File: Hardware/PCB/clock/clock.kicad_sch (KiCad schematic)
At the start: 51 parts, among them J1 Synth_power_2x5, J2 AudioJack2, J3 AudioJack2, J4 AudioJack2, J5 AudioJack2, J6 AudioJack2, J7 AudioJack2, Q1 2N3904, SW1 RotaryEncoder, SW2 SW_Push, U1 40106

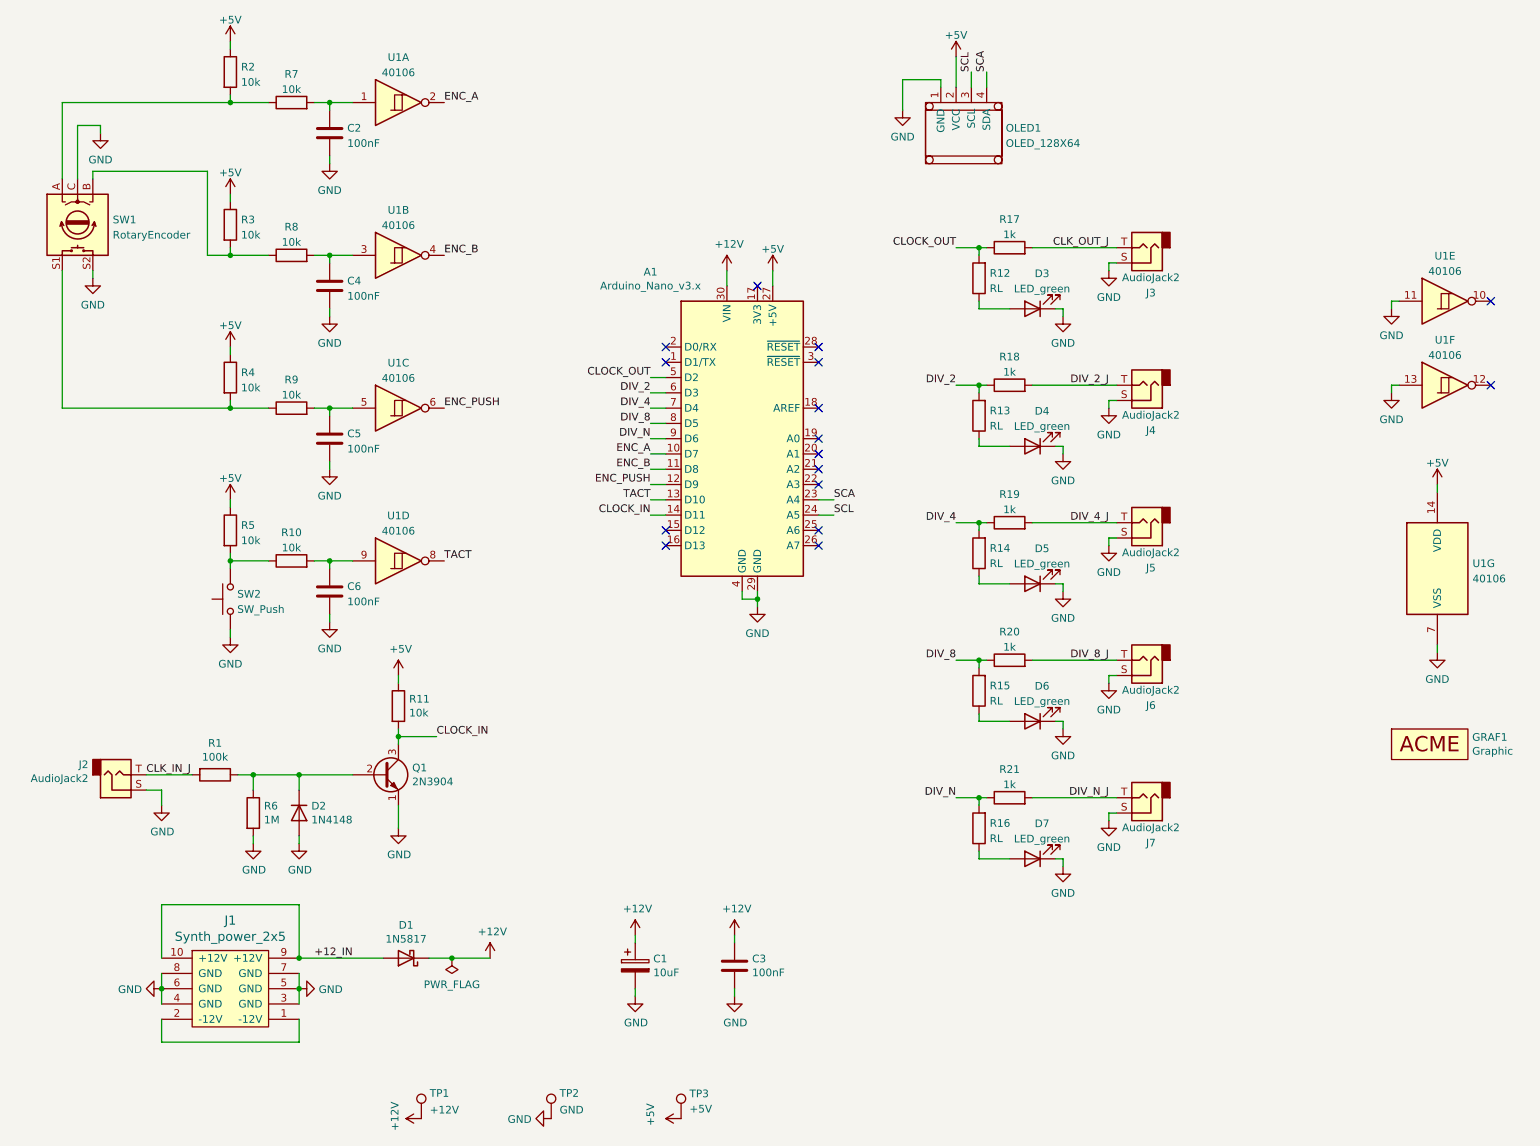
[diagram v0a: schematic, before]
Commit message: Invert clock in; fill in README; software improvements; rm notes
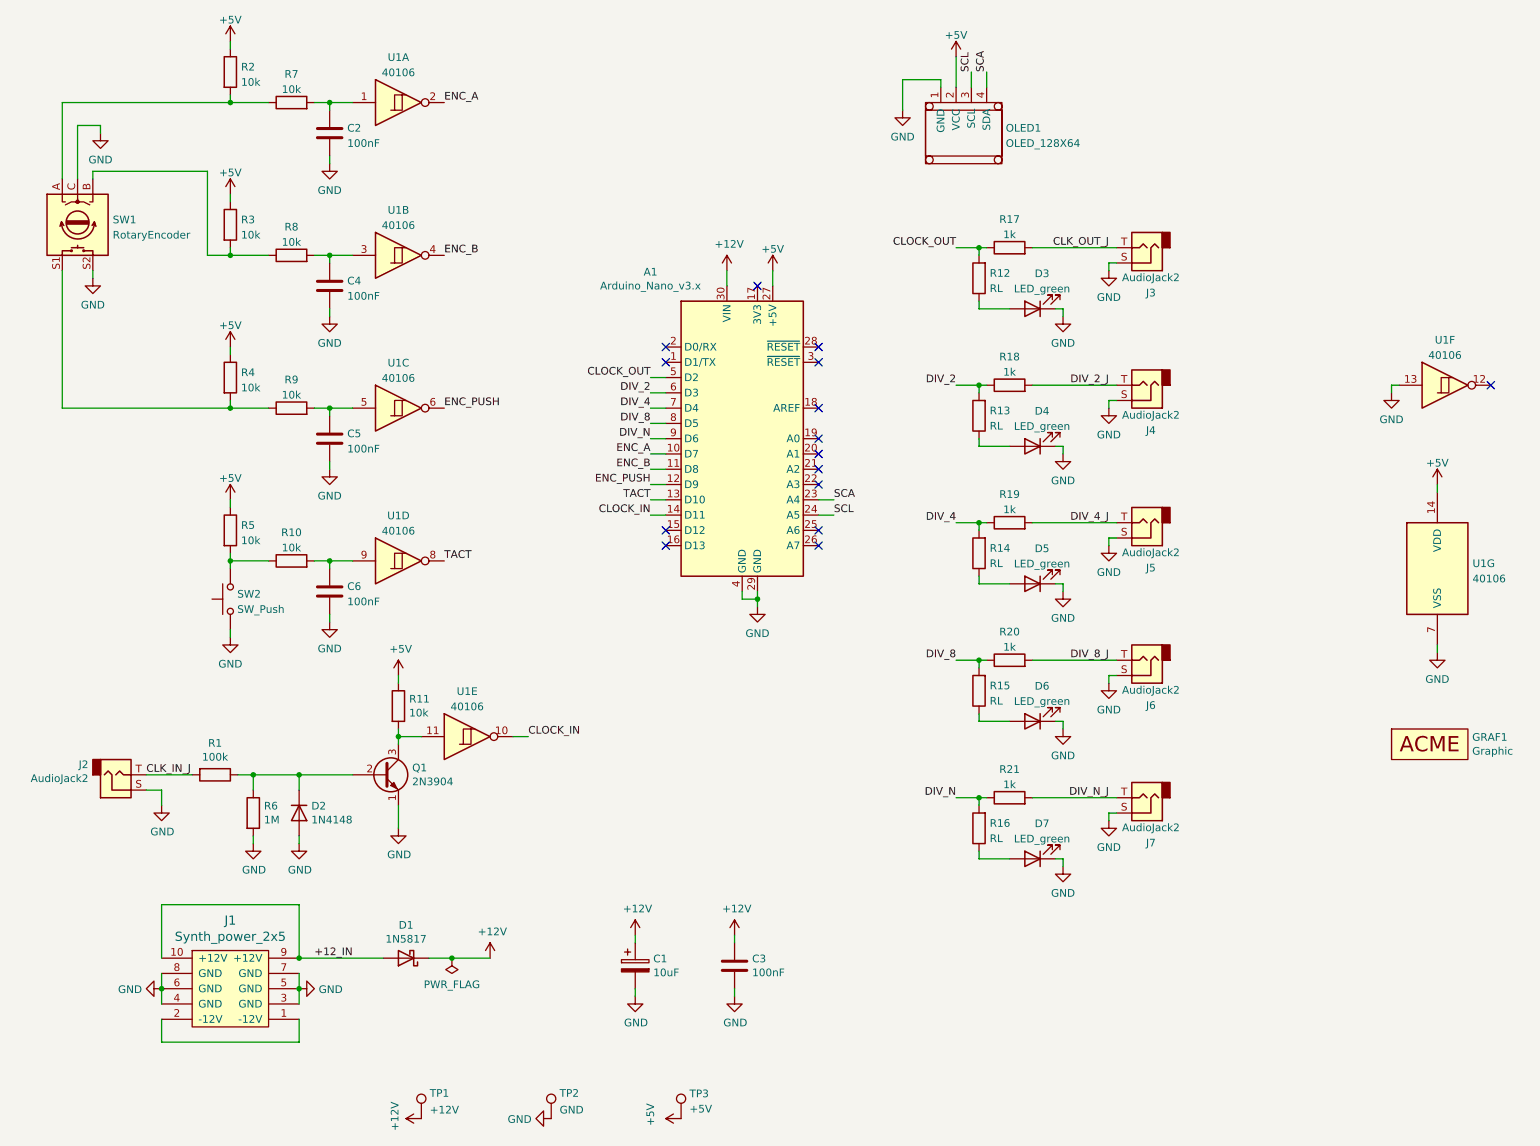
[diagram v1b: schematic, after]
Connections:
- net CLOCK_IN: now also U1.10; no longer Q1.3 (C), R11.2
- net GND: no longer U1.11
- new net: Q1.3 (C), R11.2, U1.11
- no-connect marks 16 -> 15
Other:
- moved on the sheet: U1E
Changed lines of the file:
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@@
   (no_connect (at 123.19 101.6))
   (no_connect (at 260.35 77.47))
-  (no_connect (at 260.35 63.5))
   (no_connect (at 138.43 60.96))
   (wire (pts (xy 22.86 58.42) (xy 22.86 81.28))
@@
     (stroke (width 0) (type default) (color 0 0 0 0))
   )
-  (wire (pts (xy 245.11 63.5) (xy 243.84 63.5))
-    (stroke (width 0) (type default) (color 0 0 0 0))
-  )
   (wire (pts (xy 171.45 123.19) (xy 175.26 123.19))
     (stroke (width 0) (type default) (color 0 0 0 0))
@@
     (stroke (width 0) (type default) (color 0 0 0 0))
   )
+  (wire (pts (xy 100.33 135.89) (xy 97.79 135.89))
+    (stroke (width 0) (type default) (color 0 0 0 0))
+  )
   (wire (pts (xy 50.8 118.11) (xy 50.8 119.38))
     (stroke (width 0) (type default) (color 0 0 0 0))
@@
     (stroke (width 0) (type default) (color 0 0 0 0))
   )
-  (wire (pts (xy 78.74 135.89) (xy 85.09 135.89))
+  (wire (pts (xy 78.74 135.89) (xy 82.55 135.89))
     (stroke (width 0) (type default) (color 0 0 0 0))
   )
@@
   )
   (wire (pts (xy 175.26 146.05) (xy 175.26 147.32))
-    (stroke (width 0) (type default) (color 0 0 0 0))
-  )
-  (wire (pts (xy 243.84 63.5) (xy 243.84 64.77))
     (stroke (width 0) (type default) (color 0 0 0 0))
   )
@@
     (effects (font (size 1.27 1.27)) (justify right bottom))
   )
-  (label "CLOCK_IN" (at 85.09 135.89 0)
+  (label "CLOCK_IN" (at 100.33 135.89 0)
     (effects (font (size 1.27 1.27)) (justify left bottom))
   )
@@
     (pin "1")
   )
-  (symbol (lib_id "power:GND") (at 243.84 64.77 0) (unit 1)
-    (in_bom yes) (on_board yes) (fields_autoplaced)
-    (property "Reference" "#PWR035" (id 0) (at 243.84 71.12 0)
-      (effects (font (size 1.27 1.27)) hide)
-    )
-    (property "Value" "GND" (id 1) (at 243.84 69.2134 0))
-    (property "Footprint" "" (id 2) (at 243.84 64.77 0)
-      (effects (font (size 1.27 1.27)) hide)
-    )
-    (property "Datasheet" "" (id 3) (at 243.84 64.77 0)
-      (effects (font (size 1.27 1.27)) hide)
-    )
-    (pin "1")
-  )
   (symbol (lib_id "ao_symbols:C") (at 67.31 86.36 0) (unit 1)
     (in_bom yes) (on_board yes) (fields_autoplaced)
@@
     (pin "2")
   )
-  (symbol (lib_id "4xxx:40106") (at 252.73 63.5 0) (unit 5)
-    (in_bom yes) (on_board yes) (fields_autoplaced)
-    (property "Reference" "U1" (id 0) (at 252.73 55.9902 0))
-    (property "Value" "40106" (id 1) (at 252.73 58.5271 0))
-    (property "Footprint" "" (id 2) (at 252.73 63.5 0)
-      (effects (font (size 1.27 1.27)) hide)
-    )
-    (property "Datasheet" "https://assets.nexperia.com/documents/data-sheet/HEF40106B.pdf" (id 3) (at 252.73 63.5 0)
+  (symbol (lib_id "4xxx:40106") (at 90.17 135.89 0) (unit 5)
+    (in_bom yes) (on_board yes) (fields_autoplaced)
+    (property "Reference" "U1" (id 0) (at 90.17 128.3802 0))
+    (property "Value" "40106" (id 1) (at 90.17 130.9171 0))
+    (property "Footprint" "" (id 2) (at 90.17 135.89 0)
+      (effects (font (size 1.27 1.27)) hide)
+    )
+    (property "Datasheet" "https://assets.nexperia.com/documents/data-sheet/HEF40106B.pdf" (id 3) (at 90.17 135.89 0)
       (effects (font (size 1.27 1.27)) hide)
     )
@@
       (reference "#PWR034") (unit 1) (value "GND") (footprint "")
     )
-    (path "/66e12fd8-6daa-403e-aa1e-0e8e7c3ddcbe"
-      (reference "#PWR035") (unit 1) (value "GND") (footprint "")
-    )
     (path "/562ae8ea-e68d-49c3-81d5-494d2cf00740"

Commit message: Initial layout, README update, software cleanup
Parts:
- added GRAF2: Behind, clock:clock_panel_behind, symbol ao_symbols:Graphic
- added H1, H2, H3, H4: MountingHole, ao_tht:MountingHole_3.2mm_M3, symbol ao_symbols:MountingHole
- added J8, J9: Conn_02x04_Odd_Even, Connector_IDC:IDC-Header_2x04_P2.54mm_Vertical, symbol Connector_Generic:Conn_02x04_Odd_Even
- D3, D4, D5, D6, D7: footprint (none) -> ao_tht:LED_D5.0mm
- GRAF1: value Graphic -> Holes; footprint clock:clock_panel_mockup -> clock:clock_panel_holes
- OLED1: footprint (none) -> Connector_PinHeader_2.54mm:PinHeader_1x04_P2.54mm_Vertical
- R1, R10, R11, R12, R13, R14, R15, R16, R17, R18, R19, R2, R20, R21, R3, R4, R5, R6, R7, R8, R9: footprint ao_tht:R_Axial_DIN0207_L6.3mm_D2.5mm_P10.16mm_Horizontal -> ao_tht:R_Axial_DIN0204_L3.6mm_D1.6mm_P7.62mm_Horizontal
- SW1: footprint (none) -> ao_tht:RotaryEncoder_Bourns-PEC11R-4xxxF-Sxxxx-Switch_Vertical_H20mm
- SW2: footprint (none) -> ao_tht:Tactile_E-switch_TL1100F160Q
- U1: footprint (none) -> ao_tht:DIP-14_W7.62mm_Socket_LongPads
- renumbered C2 to C1, C4 to C2, C5 to C3, C6 to C4, C1 to C5, C3 to C6, D2 to D1, D1 to D2, J2 to J1, J1 to J2
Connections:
- net +12V: no longer C6.1
- net +5V: now also C6.1, J8.3 (Pin_3); no longer OLED1.2 (VCC), R2.1, R3.1, R4.1, R5.1
- net GND: now also J8.1 (Pin_1); no longer C1.2, C2.2, C3.2, C4.2, OLED1.1 (GND), SW1.C, SW1.S2, SW2.1
- net SCA: now also J8.7 (Pin_7); no longer OLED1.4 (SDA)
- net SCL: now also J8.5 (Pin_5); no longer OLED1.3 (SCL)
- net ENC_A_JA: now reaches C1.1, R7.2
- net ENC_A_JA: now also J9.8 (Pin_8); no longer U1.1
- net TACT_JA: now reaches C4.1, R10.2
- net TACT_JA: now also J9.2 (Pin_2); no longer U1.9
- net ENC_B_JA: now reaches C2.1, R8.2
- net ENC_B_JA: now also J9.6 (Pin_6); no longer U1.3
- net CLK_OUT_L: now reaches D3.2 (A), R12.1
- net DIV_2_L: now reaches D4.2 (A), R13.1
- net DIV_8_L: now reaches D6.2 (A), R15.1
- net ENC_PUSH_JA: now reaches C3.1, R9.2
- net ENC_PUSH_JA: now also J9.4 (Pin_4); no longer U1.5
- net DIV_4_L: now reaches D5.2 (A), R14.1
- net DIV_N_L: now reaches D7.2 (A), R16.1
- new net +5V_1: J9.3 (Pin_3), OLED1.2 (VCC), R2.1, R3.1, R4.1, R5.1
- new net ENC_A_JB: J8.8 (Pin_8), U1.1
- new net ENC_B_JB: J8.6 (Pin_6), U1.3
- new net ENC_PUSH_JB: J8.4 (Pin_4), U1.5
- new net GND1: C1.2, C2.2, C3.2, C4.2, J9.1 (Pin_1), OLED1.1 (GND), SW1.C, SW1.S2, SW2.1
- new net SCA_JA: J9.7 (Pin_7), OLED1.4 (SDA)
- new net SCL_JA: J9.5 (Pin_5), OLED1.3 (SCL)
- new net TACT_JB: J8.2 (Pin_2), U1.9
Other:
- moved on the sheet: A1, C6, D1, D3, D4, D5, D6, D7, J1, J3, J4, J5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

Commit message: Layout revisions
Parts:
- GRAF2: footprint clock:clock_panel_behind -> clock:clock_panel_holes
- OLED1: footprint Connector_PinHeader_2.54mm:PinHeader_1x04_P2.54mm_Vertical -> ao_tht:OLED_MC130GX
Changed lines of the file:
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@@
       (effects (font (size 1.27 1.27)) (justify left))
     )
-    (property "Footprint" "clock:clock_panel_behind" (id 2) (at 250.19 144.78 0)
+    (property "Footprint" "clock:clock_panel_holes" (id 2) (at 250.19 144.78 0)
       (effects (font (size 1.27 1.27)) hide)
     )
@@
       (effects (font (size 1.27 1.27)) (justify left))
     )
-    (property "Footprint" "Connector_PinHeader_2.54mm:PinHeader_1x04_P2.54mm_Vertical" (id 2) (at 27.94 113.03 0)
+    (property "Footprint" "ao_tht:OLED_MC130GX" (id 2) (at 27.94 113.03 0)
       (effects (font (size 1.27 1.27)) hide)
     )
@@
     )
     (path "/3148a9e6-1e75-4e2a-b943-102cc5541cb8"
-      (reference "GRAF2") (unit 1) (value "Behind") (footprint "clock:clock_panel_behind")
+      (reference "GRAF2") (unit 1) (value "Behind") (footprint "clock:clock_panel_holes")
     )
     (path "/9aa227a4-5918-4955-a2f5-b1e4c4fe38eb"
@@
     )
     (path "/33f39dd2-4a83-487c-ae50-5387dc326ac4"
-      (reference "OLED1") (unit 1) (value "OLED_128X64") (footprint "Connector_PinHeader_2.54mm:PinHeader_1x04_P2.54mm_Vertical")
+      (reference "OLED1") (unit 1) (value "OLED_128X64") (footprint "ao_tht:OLED_MC130GX")
     )
     (path "/cc4603d6-fbbe-4d4f-8c75-cc951d37e1ff"
